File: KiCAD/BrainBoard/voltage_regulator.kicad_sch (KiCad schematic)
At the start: 3 parts, among them U1 LM2940IMPX-5.0/NOPB

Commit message: [docs] update page settings
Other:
- company: (none) -> Nathan Wignall
- title: (none) -> Voltage Regulator
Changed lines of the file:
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@@
 	(generator_version "9.0")
 	(paper "A4")
+	(title_block
+		(title "Voltage Regulator")
+		(date "${CURRENT_DATE}")
+		(company "Nathan Wignall")
+	)
 	(text "aluminum electrolytic or tantalum\nESR = 100mΩ to 1Ω\nsee datasheet"
 		(exclude_from_sim no)

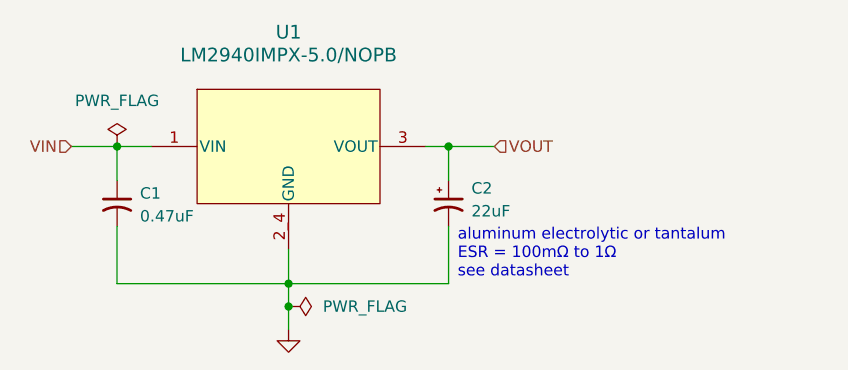
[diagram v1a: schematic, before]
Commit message: [fix] replace linear regulator
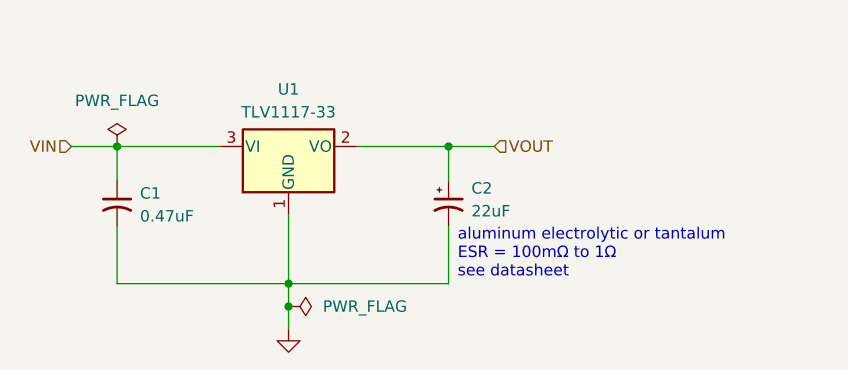
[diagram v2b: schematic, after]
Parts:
- removed U1: LM2940IMPX-5.0/NOPB, Project Footprints:LM2940IMPX_5.0NOPB, symbol LM2940IMPX_5.0NOPB:LM2940IMPX-5.0_NOPB
- added U1: TLV1117-33, symbol Regulator_Linear:TLV1117-33
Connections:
- net GND: now also U1.1 (GND)
- net VIN: now also U1.3 (VI)
- net VOUT: now also U1.2 (VO)
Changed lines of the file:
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@@
-	(wire
-		(pts
-			(xy 153.67 93.98) (xy 156.21 93.98)
-		)
-		(stroke
-			(width 0)
-			(type default)
-		)
-	)
 	(wire
 		(pts
@@
 	(wire
 		(pts
-			(xy 119.38 93.98) (xy 123.19 93.98)
+			(xy 119.38 93.98) (xy 130.81 93.98)
 		)
 		(stroke
@@
 	(wire
 		(pts
-			(xy 138.43 109.22) (xy 138.43 105.41)
+			(xy 146.05 93.98) (xy 156.21 93.98)
+		)
+		(stroke
+			(width 0)
+			(type default)
+		)
+	)
+	(wire
+		(pts
+			(xy 138.43 101.6) (xy 138.43 109.22)
 		)
 		(stroke
@@
 			)
 			(justify left)
+		)
+	)
+	(symbol
+		(lib_id "Regulator_Linear:TLV1117-33")
+		(at 138.43 93.98 0)
+		(unit 1)
+		(exclude_from_sim no)
+		(in_bom yes)
+		(on_board yes)
+		(dnp no)
+		(fields_autoplaced yes)
+		(property "Reference" "U1"
+			(at 138.43 87.63 0)
+			(effects
+				(font
+					(size 1.27 1.27)
+				)
+			)
+		)
+		(property "Value" "TLV1117-33"
+			(at 138.43 90.17 0)
+			(effects
+				(font
+					(size 1.27 1.27)
+				)
+			)
+		)
+		(property "Footprint" ""
+			(at 138.43 93.98 0)
+			(effects
+				(font
+					(size 1.27 1.27)
+				)
+				(hide yes)
+			)
+		)
+		(property "Datasheet" "http://www.ti.com/lit/ds/symlink/tlv1117.pdf"
+			(at 138.43 93.98 0)
+			(effects
+				(font
+					(size 1.27 1.27)
+				)
+				(hide yes)
+			)
+		)
+		(property "Description" "800mA Low-Dropout Linear Regulator, 3.3V fixed output, TO-220/TO-252/TO-263/SOT-223"
+			(at 138.43 93.98 0)
+			(effects
+				(font
+					(size 1.27 1.27)
+				)
+				(hide yes)
+			)
+		)
+		(pin "3"
+		)
+		(pin "1"
+		)
+		(pin "2"
+		)
+		(instances
+			(project ""
+				(path "/44e391a9-9312-4881-bf0a-d93a44472e34/8dbe2292-b9b2-4749-8512-0e3dddbd3bdc"
+					(reference "U1")
+					(unit 1)
+				)
+			)
 		)
 	)
@@
 					(unit 1)
 				)
-			)
-		)
-	)
-	(symbol
-		(lib_id "LM2940IMPX_5.0NOPB:LM2940IMPX-5.0_NOPB")
-		(at 138.43 93.98 0)
-		(unit 1)
-		(exclude_from_sim no)
-		(in_bom yes)
-		(on_board yes)
-		(dnp no)
-		(fields_autoplaced yes)
-		(property "Reference" "U1"
-			(at 138.43 81.28 0)
-			(effects
-				(font
-					(size 1.524 1.524)
-				)
-			)
-		)
-		(property "Value" "LM2940IMPX-5.0/NOPB"
-			(at 138.43 83.82 0)
-			(effects
-				(font
-					(size 1.524 1.524)
-				)
-			)
-		)
-		(property "Footprint" "Project Footprints:LM2940IMPX_5.0NOPB"
-			(at 138.43 93.98 0)
-			(effects
-				(font
-					(size 1.27 1.27)
-					(italic yes)
-				)
-				(hide yes)
-			)
-		)
-		(property "Datasheet" "https://www.ti.com/lit/gpn/lm2940-n"
-			(at 138.43 93.98 0)
-			(effects
-				(font
-					(size 1.27 1.27)
-					(italic yes)
-				)
-				(hide yes)
-			)
-		)
-		(property "Description" ""
-			(at 138.43 93.98 0)
-			(effects
-				(font
-					(size 1.27 1.27)
-				)
-				(hide yes)
-			)
-		)
-		(pin "3"
-		)
-		(pin "1"
-		)
-		(pin "2_4"
-		)
-		(instances
-			(project "BrainBoard"
-				(path "/44e391a9-9312-4881-bf0a-d93a44472e34/8dbe2292-b9b2-4749-8512-0e3dddbd3bdc"
-					(reference "U1")
-					(unit 1)
-				)
